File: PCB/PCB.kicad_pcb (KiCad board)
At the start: 2 copper layers, 46 x 32.5 mm, 62 parts, among them J1 AudioJack3, J2 USB4105-GF-A, J4 Conn_01x09, U1 ADP151AUJZ-3.3-R7, U2 MAX41400ATB+T, U3 AD8534ARZ, U6 AD8534ARZ

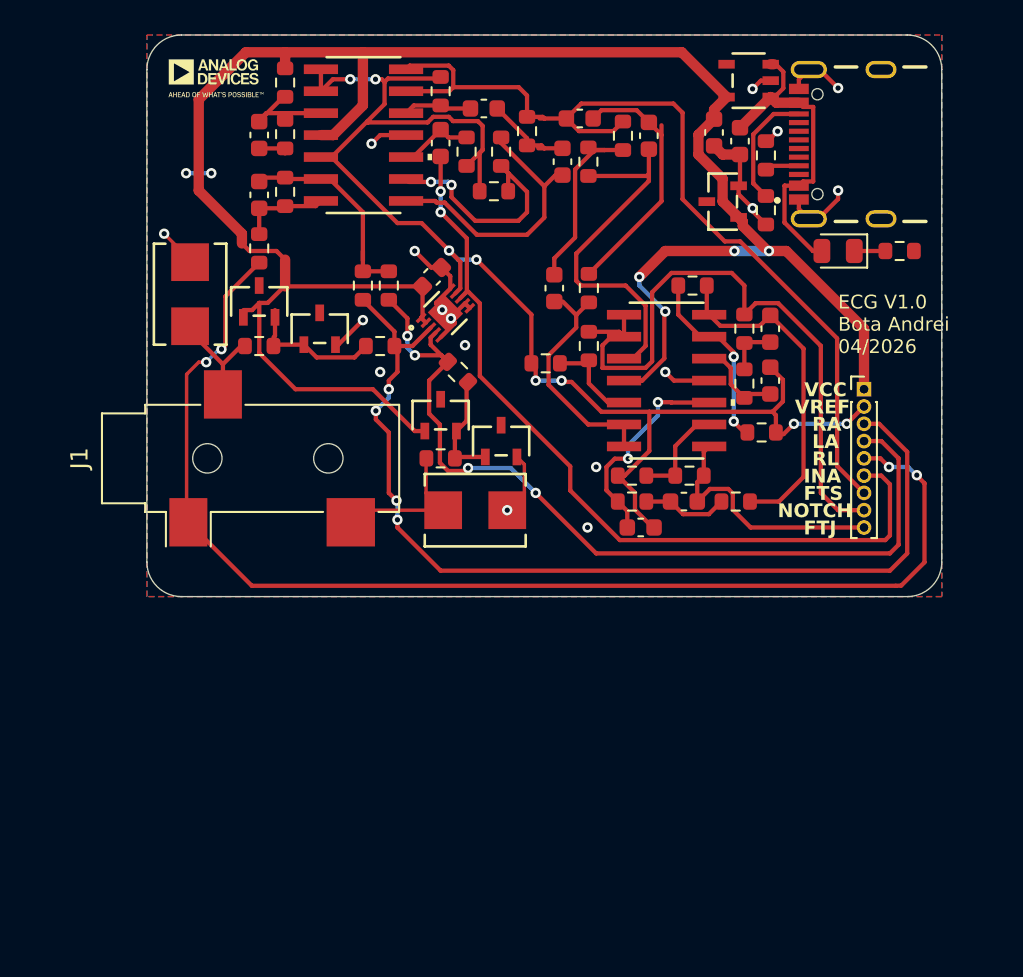
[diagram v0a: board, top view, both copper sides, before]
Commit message: Modificat pcb ul cu scopul de a adauga test point uri
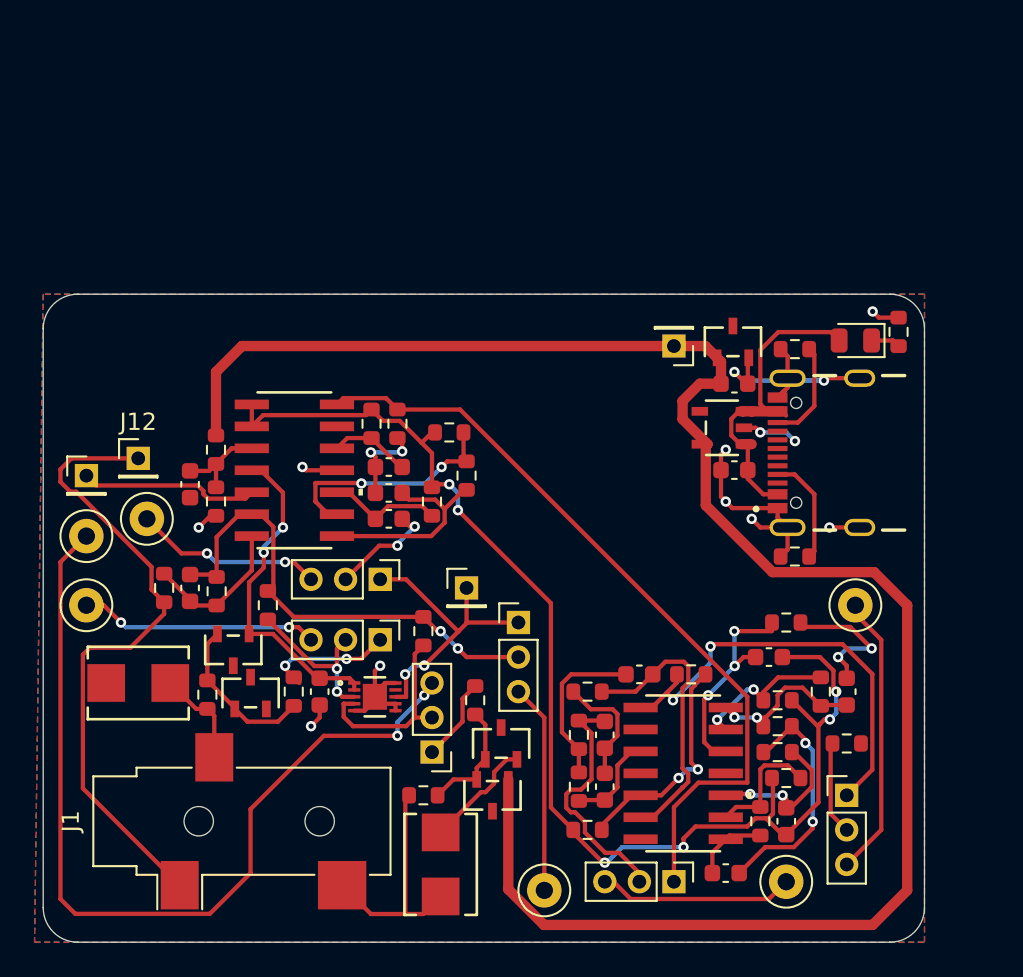
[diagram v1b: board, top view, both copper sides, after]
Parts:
- removed G***: LOGO, ADlogo:adlogo
- added J10: Conn_01x01_Pin, Connector_PinHeader_2.00mm:PinHeader_1x01_P2.00mm_Vertical, F.Cu at (105.5, 126.5)
- added J11: Conn_01x01_Pin, Connector_PinHeader_2.00mm:PinHeader_1x01_P2.00mm_Vertical, F.Cu at (139.5, 119.0)
- added J12: Conn_01x01_Pin, Connector_PinHeader_2.00mm:PinHeader_1x01_P2.00mm_Vertical, F.Cu at (108.5, 125.5)
- added J3: Conn_01x03_Pin, Connector_PinHeader_2.00mm:PinHeader_1x03_P2.00mm_Vertical, F.Cu at (139.5, 150.0)
- added J5: Conn_01x03_Pin, Connector_PinHeader_2.00mm:PinHeader_1x03_P2.00mm_Vertical, F.Cu at (125.5, 142.5)
- added J6: Conn_01x03_Pin, Connector_PinHeader_2.00mm:PinHeader_1x03_P2.00mm_Vertical, F.Cu at (122.5, 136.0)
- added J7: Conn_01x03_Pin, Connector_PinHeader_2.00mm:PinHeader_1x03_P2.00mm_Vertical, F.Cu at (130.5, 135.0)
- added J8: Conn_01x03_Pin, Connector_PinHeader_2.00mm:PinHeader_1x03_P2.00mm_Vertical, F.Cu at (149.5, 145.0)
- added J9: Conn_01x01_Pin, Connector_PinHeader_2.00mm:PinHeader_1x01_P2.00mm_Vertical, F.Cu at (127.5, 133.0)
- added TP1: TestPoint, TestPoint:TestPoint_Loop_D2.50mm_Drill1.0mm_LowProfile, F.Cu at (146.0, 150.0)
- added TP2: TestPoint, TestPoint:TestPoint_Loop_D2.50mm_Drill1.0mm_LowProfile, F.Cu at (109.0, 129.0)
- added TP3: TestPoint, TestPoint:TestPoint_Loop_D2.50mm_Drill1.0mm_LowProfile, F.Cu at (105.5, 130.0)
- added TP4: TestPoint, TestPoint:TestPoint_Loop_D2.50mm_Drill1.0mm_LowProfile, F.Cu at (105.5, 134.0)
- added TP5: TestPoint, TestPoint:TestPoint_Loop_D2.50mm_Drill1.0mm_LowProfile, F.Cu at (132.0, 150.5)
- added TP6: TestPoint, TestPoint:TestPoint_Loop_D2.50mm_Drill1.0mm_LowProfile, F.Cu at (150.0, 134.0)
- J4: value Conn_01x09 -> Conn_01x03_Pin; footprint Connector_PinHeader_1.00mm:PinHeader_1x09_P1.00mm_Vertical -> Connector_PinHeader_2.00mm:PinHeader_1x03_P2.00mm_Vertical
- moved C10 37.8 mm to (135.5, 144.5)
- moved R17 36.2 mm to (134.0, 144.5)
- moved C6 35.7 mm to (135.5, 141.5), turned to -90 degrees
- moved R16 34.8 mm to (134.0, 141.5)
- moved J4 30.1 mm to (122.5, 132.5), turned to -90 degrees
- moved R20 27.1 mm to (134.5, 147.0)
- moved C4 24.9 mm to (119.0, 139.0), turned to -90 degrees
- moved R21 24.7 mm to (149.5, 142.0), turned to 0 degrees
- moved R23 24.6 mm to (148.0, 139.0), turned to 90 degrees
- moved R9 23.4 mm to (113.0, 133.2)
- moved R18 23.4 mm to (134.5, 139.0), turned to 0 degrees
- moved R30 23.3 mm to (146.5, 131.2), turned to 0 degrees
- moved C5 23.1 mm to (111.5, 133.0)
- moved C11 22.9 mm to (137.5, 138.0), turned to 180 degrees
- moved U6 22.8 mm to (140.0, 143.7)
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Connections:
- net VCM renamed VCM_IN
- C6 pad 1: FTS -> NOTCH_IN
- C9 pad 2: OutIna -> FTS_IN
- J4 pad 1: Vcc -> OutIna
- J4 pad 2: Vref -> FTS_IN
- J4 pad 3: RAF -> SemnalTestFts
- R16 pad 2: FTS -> NOTCH_IN
- R21 pad 1: NOTCH -> FTJ_IN
- R7 pad 2: LAF -> INAL_IN
- R8 pad 2: RAF -> INAR_IN
- U2 pad 3: RAF -> INAR_IN
- U2 pad 4: LAF -> INAL_IN
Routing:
- net SemnalTestLA: track 0.00 -> 51.8 mm, vias 0 -> 2
- net RAF: track 57.6 -> 7.46 mm, vias 4 -> 2
- net LAF: track 51.2 -> 4.86 mm, vias 4 -> 0
- net RL: track 70.5 -> 37.2 mm, vias 4 -> 0
- net OutIna: track 47.5 -> 17.5 mm
- net SemnalTestFTJ: track 0.00 -> 15.9 mm
- net Net-(U6-+INA): track 21.4 -> 5.51 mm
- net VCM_IN: track 12.7 -> 28.0 mm, vias 0 -> 2
- net NOTCH_IN: track 0.00 -> 14.7 mm
- net SemnalTestRA: track 0.00 -> 13.8 mm, vias 0 -> 2
- net NOTCH: track 38.1 -> 25.5 mm, vias 0 -> 2
- net SemnalTestRL: track 0.00 -> 12.1 mm
- net INAL_IN: track 0.00 -> 11.3 mm
- net GND: track 41.5 -> 52.5 mm, vias 19 -> 13
- net SemnalTestFts: track 0.00 -> 10.9 mm, vias 0 -> 2
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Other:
- board size 46 x 32.5 mm -> 51 x 37.5 mm
- board text removed: "ECG V1.0 Bota Andrei 04/2026"
- board text removed: "FTJ"
- board text removed: "FTS"
- board text removed: "INA"
- board text removed: "LA"
- board text removed: "NOTCH"
- board text removed: "RA"
- board text removed: "RL"
- board text removed: "VCC"
- board text removed: "VREF"

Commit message: Modificat pcb
Signed-off-by: Andrei Bota <botaandrei69@yahoo.com>
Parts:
- removed J9: Conn_01x01_Pin, Connector_PinHeader_2.00mm:PinHeader_1x01_P2.00mm_Vertical
- removed TP1, TP2, TP3, TP4, TP5, TP6: TestPoint, TestPoint:TestPoint_Loop_D2.50mm_Drill1.0mm_LowProfile
- added G***: LOGO, ADlogo:adlogo, F.Cu at (155.0, 148.5)
- added J13: Conn_01x01_Pin, Connector_PinHeader_2.00mm:PinHeader_1x01_P2.00mm_Vertical, F.Cu at (153.5, 142.1)
- added J14: Conn_01x01_Pin, Connector_PinHeader_2.00mm:PinHeader_1x01_P2.00mm_Vertical, F.Cu at (147.5, 134.1)
- added J15: Conn_01x01_Pin, Connector_PinHeader_2.00mm:PinHeader_1x01_P2.00mm_Vertical, F.Cu at (158.0, 133.1)
- added J16: Conn_01x01_Pin, Connector_PinHeader_2.00mm:PinHeader_1x01_P2.00mm_Vertical, F.Cu at (157.5, 136.1)
- added J17: Conn_01x01_Pin, Connector_PinHeader_2.00mm:PinHeader_1x01_P2.00mm_Vertical, F.Cu at (146.5, 119.0)
- added J18: Conn_01x01_Pin, Connector_PinHeader_2.00mm:PinHeader_1x01_P2.00mm_Vertical, F.Cu at (167.5, 125.0)
- added J19: Conn_01x01_Pin, Connector_PinHeader_2.00mm:PinHeader_1x01_P2.00mm_Vertical, F.Cu at (159.5, 129.6)
- moved R20 38.9 mm to (159.5, 117.2), turned to 0 degrees
- moved J11 34.0 mm to (168.8, 136.1), turned to -90 degrees
- moved J8 32.9 mm to (167.5, 117.5)
- moved C15 29.7 mm to (163.5, 128.6), turned to 90 degrees
- moved R29 29.5 mm to (161.3, 144.6), turned to 90 degrees
- moved C10 29.1 mm to (154.5, 122.5)
- moved C6 29.1 mm to (154.5, 119.5)
- moved R16 28.9 mm to (153.0, 119.7)
- moved R17 28.8 mm to (153.0, 122.9)
- moved J3 28.8 mm to (149.5, 123.0), turned to 180 degrees
- moved D1 28.7 mm to (160.8, 141.1), turned to 90 degrees
- moved R27 28.5 mm to (163.5, 125.2)
- moved R21 28.4 mm to (162.5, 116.7)
- moved U6 28.3 mm to (159.0, 122.7)
- moved J4 28.2 mm to (150.5, 136.1), turned to 90 degrees
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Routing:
- net SemnalTestLA: track 51.8 -> 3.21 mm, vias 2 -> 0
- net FTS: track 45.2 -> 12.6 mm
- net Vcc: track 125.3 -> 151.7 mm, vias 2 -> 8
- net INAL_IN: track 11.3 -> 33.1 mm, vias 0 -> 2
- net RL: track 37.2 -> 22.3 mm
- net FTS_IN: track 6.24 -> 19.5 mm
- net SemnalTestFTJ: track 15.9 -> 3.50 mm
- net GND: track 52.5 -> 40.7 mm, vias 13 -> 10
- net Net-(U6--INB): track 16.4 -> 5.10 mm
- net SemnalTestRA: track 13.8 -> 3.00 mm, vias 2 -> 0
- net NOTCH: track 25.5 -> 15.3 mm, vias 2 -> 0
- net OutIna: track 17.5 -> 7.59 mm, vias 2 -> 0
- net SemnalTestRL: track 12.1 -> 3.00 mm
- net INAR_IN: track 9.51 -> 18.5 mm, vias 2 -> 0
- net NOTCH_IN: track 14.7 -> 5.96 mm
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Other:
- board size 51 x 37.5 mm -> 43 x 38 mm
- board text added: "Bota Andrei Rev A 04/2026"
- board text added: "FTJ"
- board text added: "FTS"
- board text added: "IA"
- board text added: "LA"
- board text added: "NOTCH"
- board text added: "RA"
- board text added: "RL"
- board text added: "VCM"
- board text added: "VREF"

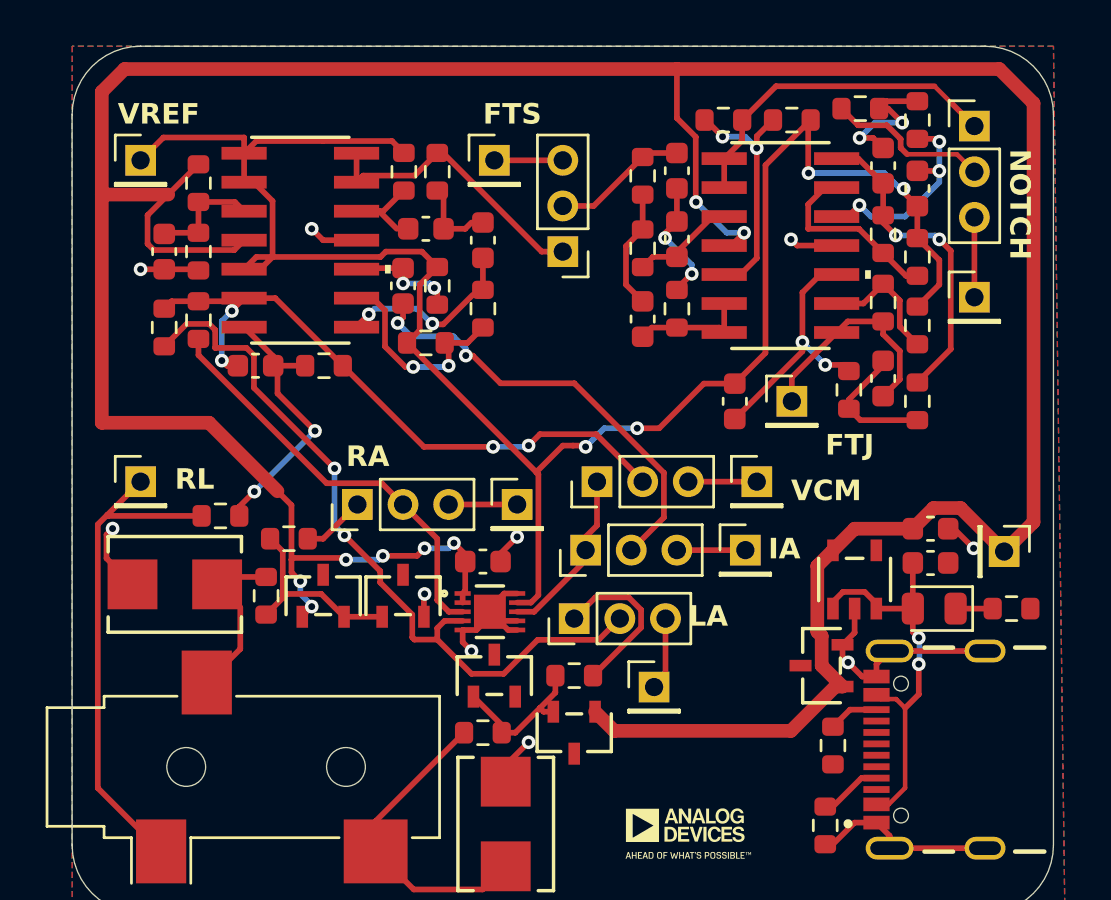
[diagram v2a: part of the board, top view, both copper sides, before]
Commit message: Remodificat un pin de testpoint
Signed-off-by: BotaAndreiD <botaandrei69@yahoo.com>
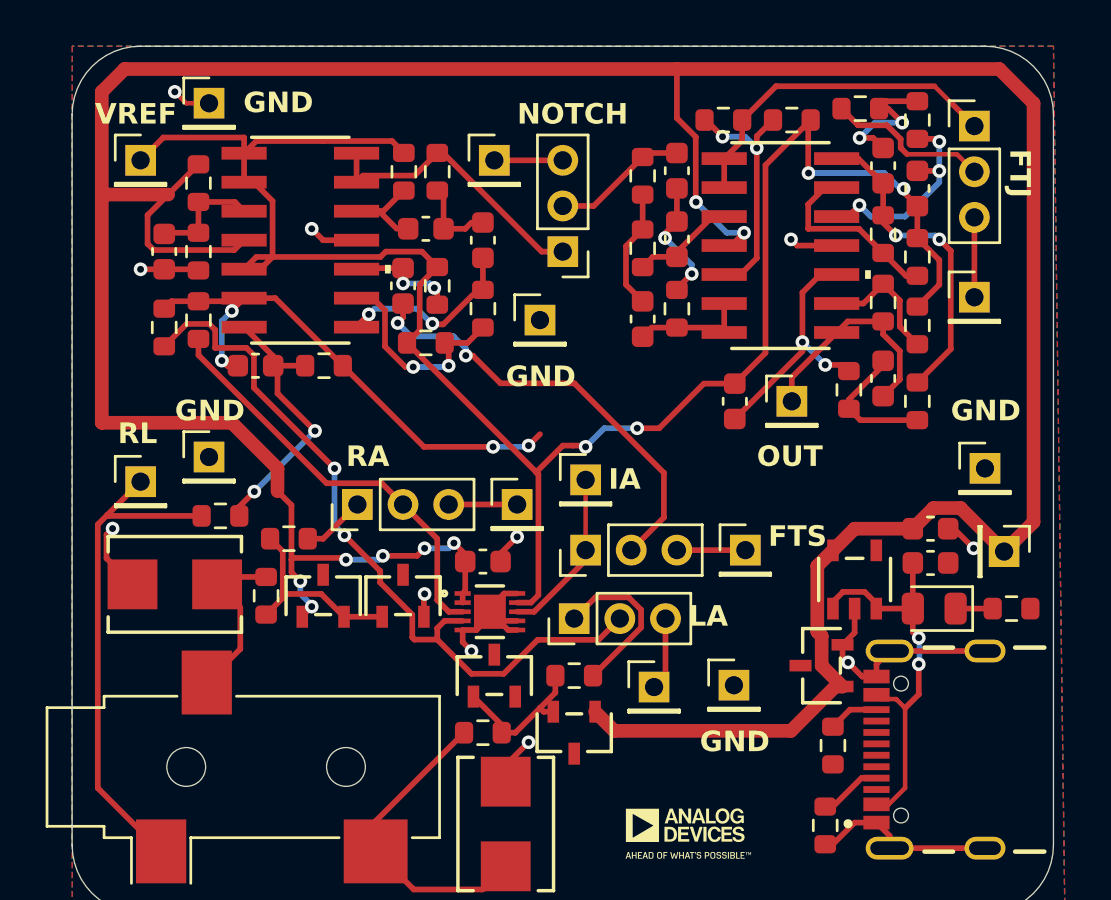
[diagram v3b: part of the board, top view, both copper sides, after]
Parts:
- removed J15: Conn_01x01_Pin, Connector_PinHeader_2.00mm:PinHeader_1x01_P2.00mm_Vertical
- added J20: Conn_01x01_Pin, Connector_PinHeader_2.00mm:PinHeader_1x01_P2.00mm_Vertical, F.Cu at (168.0, 132.5)
- added J21: Conn_01x01_Pin, Connector_PinHeader_2.00mm:PinHeader_1x01_P2.00mm_Vertical, F.Cu at (134.0, 116.5)
- added J22: Conn_01x01_Pin, Connector_PinHeader_2.00mm:PinHeader_1x01_P2.00mm_Vertical, F.Cu at (134.0, 132.0)
- added J24: Conn_01x01_Pin, Connector_PinHeader_2.00mm:PinHeader_1x01_P2.00mm_Vertical, F.Cu at (148.5, 126.0)
- added J9: Conn_01x01_Pin, Connector_PinHeader_2.00mm:PinHeader_1x01_P2.00mm_Vertical, F.Cu at (157.0, 142.0)
- J7: value Conn_01x03_Pin -> Conn_01x01_Pin; footprint Connector_PinHeader_2.00mm:PinHeader_1x03_P2.00mm_Vertical -> Connector_PinHeader_2.00mm:PinHeader_1x01_P2.00mm_Vertical
- moved J7 0.51 mm to (150.5, 133.0), turned to 0 degrees
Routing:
- net VCM_IN: track 28.9 -> 23.5 mm
- net SemnalTestRL: track 3.00 -> 0.00 mm
- net GND: track 40.7 -> 42.4 mm, vias 10 -> 11
- net Vcc: track 151.7 -> 152.2 mm
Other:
- board text added: "GND"
- board text added: "OUT"
- board text removed: "VCM"

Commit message: Ultimele modificari a iteratiei A pentru PCB inainte de comanda
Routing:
- net VCM_IN: track 23.5 -> 13.2 mm, vias 4 -> 2
- net FTS_IN: track 19.5 -> 17.6 mm

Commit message: Adaugat adc si uc la pcb
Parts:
- added C16: 100n, Capacitor_SMD:C_1206_3216Metric_Pad1.33x1.80mm_HandSolder, F.Cu at (178.4, 102.2)
- added C17: 100n, Capacitor_SMD:C_1206_3216Metric_Pad1.33x1.80mm_HandSolder, F.Cu at (178.4, 105.6)
- added C18: 1u, Capacitor_SMD:C_1206_3216Metric_Pad1.33x1.80mm_HandSolder, F.Cu at (178.4, 109.0)
- added C19: 100n, Capacitor_SMD:C_1206_3216Metric_Pad1.33x1.80mm_HandSolder, F.Cu at (178.4, 112.3)
- added C20: 100n, Capacitor_SMD:C_1206_3216Metric_Pad1.33x1.80mm_HandSolder, F.Cu at (178.4, 115.7)
- added C21: 100n, Capacitor_SMD:C_1206_3216Metric_Pad1.33x1.80mm_HandSolder, F.Cu at (178.4, 119.0)
- added J15: Conn_01x03_Pin, Connector_PinSocket_2.54mm:PinSocket_1x08_P2.54mm_Vertical, B.Cu at (243.0, 138.2)
- added U4: AD7124-4BRUZ, footprints:RU-24_ADI-L, F.Cu at (218.8, 147.7)
- added U5: ESP32-C3_SUPERMINI_TH, footprints:MODULE_ESP32-C3_SUPERMINI_TH, F.Cu at (235.4, 148.1)
- C1, C10, C12, C13, C14, C15, C2, C3, C4, C5, C6, C7, C8, C9: footprint Capacitor_SMD:C_0603_1608Metric -> Capacitor_SMD:C_1206_3216Metric_Pad1.33x1.80mm_HandSolder
- C11: value 200n -> 220n; footprint Capacitor_SMD:C_0603_1608Metric -> Capacitor_SMD:C_1206_3216Metric_Pad1.33x1.80mm_HandSolder
- J10, J11, J12, J13, J14, J16, J17, J18, J19, J20, J21, J24, J7, J9: footprint Connector_PinHeader_2.00mm:PinHeader_1x01_P2.00mm_Vertical -> Connector_PinHeader_2.54mm:PinHeader_1x03_P2.54mm_Vertical
- J3, J4, J5, J6, J8: footprint Connector_PinHeader_2.00mm:PinHeader_1x03_P2.00mm_Vertical -> Connector_PinHeader_2.54mm:PinHeader_1x03_P2.54mm_Vertical
- R1, R10, R11, R12, R13, R14, R15, R16, R17, R18, R19, R2, R20, R21, R22, R23, R24, R25, R26, R27, R29, R3, R30, R31, R4, R5, R6, R7, R8, R9: footprint Resistor_SMD:R_0603_1608Metric -> Resistor_SMD:R_1206_3216Metric_Pad1.30x1.75mm_HandSolder
- R28: footprint Resistor_SMD:R_0603_1608Metric -> Capacitor_SMD:C_0603_1608Metric
- moved J22 95.2 mm to (227.8, 148.3)
- moved J16 19.1 mm to (175.5, 142.5)
- moved J20 6.08 mm to (174.0, 131.5)
- moved J10 2.55 mm to (130.5, 121.5)
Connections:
- net LAF renamed DCPOT-
- net RAF renamed DCPOT+
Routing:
- net (no net): track 0.00 -> 10.1 mm
- net MISO: track 0.00 -> 8.68 mm
- net DCPOT-: track 7.30 -> 0.00 mm
- net DCPOT+: track 2.80 -> 0.00 mm
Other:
- board size 43 x 38 mm -> 130.5 x 46.5 mm
